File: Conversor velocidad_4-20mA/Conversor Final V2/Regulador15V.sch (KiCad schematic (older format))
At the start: 4 parts

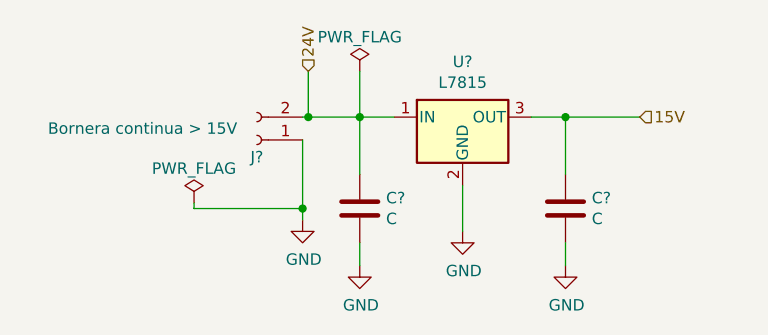
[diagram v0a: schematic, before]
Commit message: Modificacion
Modifique los esquematicos para que no de tanto error. Igualmente da error de puenteo de salidas entre las compuertas "OR" y 2 errores mas en el regulador
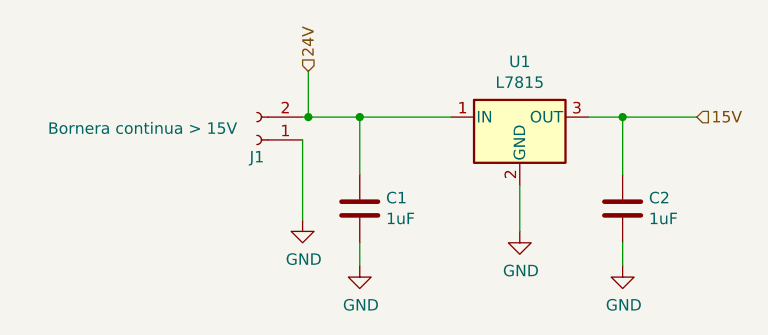
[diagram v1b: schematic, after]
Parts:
- C1, C2: renamed from C?; value C -> 1uF
- gave numbers to parts that had none: 2
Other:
- moved on the sheet: C2, U1
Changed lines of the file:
@@
 $EndDescr
 $Comp
-L Regulator_Linear:L7815 U?
+L Regulator_Linear:L7815 U1
 U 1 1 612EE8D8
-P 5625 3200
-F 0 "U?" H 5625 3442 50  0000 C CNN
-F 1 "L7815" H 5625 3351 50  0000 C CNN
-F 2 "" H 5650 3050 50  0001 L CIN
-F 3 "http://www.st.com/content/ccc/resource/technical/document/datasheet/41/4f/b3/b0/12/d4/47/88/CD00000444.pdf/files/CD00000444.pdf/jcr:content/translations/en.CD00000444.pdf" H 5625 3150 50  0001 C CNN
-	1    5625 3200
+P 5875 3200
+F 0 "U1" H 5875 3442 50  0000 C CNN
+F 1 "L7815" H 5875 3351 50  0000 C CNN
+F 2 "" H 5900 3050 50  0001 L CIN
+F 3 "http://www.st.com/content/ccc/resource/technical/document/datasheet/41/4f/b3/b0/12/d4/47/88/CD00000444.pdf/files/CD00000444.pdf/jcr:content/translations/en.CD00000444.pdf" H 5875 3150 50  0001 C CNN
+	1    5875 3200
 	1    0    0    -1
 $EndComp
 $Comp
-L power:GND #PWR?
+L power:GND #PWR0112
 U 1 1 612EE8DE
-P 5625 3700
-F 0 "#PWR?" H 5625 3450 50  0001 C CNN
-F 1 "GND" H 5630 3527 50  0000 C CNN
-F 2 "" H 5625 3700 50  0001 C CNN
-F 3 "" H 5625 3700 50  0001 C CNN
-	1    5625 3700
+P 5875 3700
+F 0 "#PWR0112" H 5875 3450 50  0001 C CNN
+F 1 "GND" H 5880 3527 50  0000 C CNN
+F 2 "" H 5875 3700 50  0001 C CNN
+F 3 "" H 5875 3700 50  0001 C CNN
+	1    5875 3700
 	1    0    0    -1
 $EndComp
 $Comp
-L Device:C C?
+L Device:C C1
 U 1 1 612EE8E4
 P 5175 3600
-F 0 "C?" H 5290 3646 50  0000 L CNN
-F 1 "C" H 5290 3555 50  0000 L CNN
+F 0 "C1" H 5290 3646 50  0000 L CNN
+F 1 "1uF" H 5290 3555 50  0000 L CNN
 F 2 "" H 5213 3450 50  0001 C CNN
 F 3 "~" H 5175 3600 50  0001 C CNN
@@
 $EndComp
 $Comp
-L Device:C C?
+L Device:C C2
 U 1 1 612EE8EA
-P 6075 3600
-F 0 "C?" H 6190 3646 50  0000 L CNN
-F 1 "C" H 6190 3555 50  0000 L CNN
-F 2 "" H 6113 3450 50  0001 C CNN
-F 3 "~" H 6075 3600 50  0001 C CNN
-	1    6075 3600
+P 6325 3600
+F 0 "C2" H 6440 3646 50  0000 L CNN
+F 1 "1uF" H 6440 3555 50  0000 L CNN
+F 2 "" H 6363 3450 50  0001 C CNN
+F 3 "~" H 6325 3600 50  0001 C CNN
+	1    6325 3600
 	1    0    0    -1
 $EndComp
 $Comp
-L Connector:Conn_01x02_Female J?
+L Connector:Conn_01x02_Female J1
 U 1 1 612EE8F0
 P 4725 3300
-F 0 "J?" H 4725 3375 50  0000 C CNN
+F 0 "J1" H 4725 3375 50  0000 C CNN
 F 1 "Bornera continua > 15V" H 5225 3250 50  0000 C CNN
 F 2 "" H 4725 3300 50  0001 C CNN
@@
 $EndComp
 Wire Wire Line
-	5325 3200 5175 3200
+	5175 3450 5175 3200
 Wire Wire Line
-	5175 3450 5175 3200
-Connection ~ 5175 3200
-Wire Wire Line
-	6075 3200 6075 3450
+	6325 3200 6325 3450
 $Comp
-L power:GND #PWR?
+L power:GND #PWR0113
 U 1 1 612EE8FB
-P 6075 3850
-F 0 "#PWR?" H 6075 3600 50  0001 C CNN
-F 1 "GND" H 6080 3677 50  0000 C CNN
-F 2 "" H 6075 3850 50  0001 C CNN
-F 3 "" H 6075 3850 50  0001 C CNN
-	1    6075 3850
+P 6325 3850
+F 0 "#PWR0113" H 6325 3600 50  0001 C CNN
+F 1 "GND" H 6330 3677 50  0000 C CNN
+F 2 "" H 6325 3850 50  0001 C CNN
+F 3 "" H 6325 3850 50  0001 C CNN
+	1    6325 3850
 	1    0    0    -1
 $EndComp
 $Comp
-L power:GND #PWR?
+L power:GND #PWR0114
 U 1 1 612EE901
 P 5175 3850
-F 0 "#PWR?" H 5175 3600 50  0001 C CNN
+F 0 "#PWR0114" H 5175 3600 50  0001 C CNN
 F 1 "GND" H 5180 3677 50  0000 C CNN
 F 2 "" H 5175 3850 50  0001 C CNN
@@
 $EndComp
 Wire Wire Line
-	5625 3500 5625 3700
+	5875 3500 5875 3700
 Wire Wire Line
-	6075 3750 6075 3850
+	6325 3750 6325 3850
 Wire Wire Line
 	5175 3750 5175 3850
 $Comp
-L power:GND #PWR?
+L power:GND #PWR0115
 U 1 1 612EE90B
 P 4925 3650
-F 0 "#PWR?" H 4925 3400 50  0001 C CNN
+F 0 "#PWR0115" H 4925 3400 50  0001 C CNN
 F 1 "GND" H 4930 3477 50  0000 C CNN
 F 2 "" H 4925 3650 50  0001 C CNN
 F 3 "" H 4925 3650 50  0001 C CNN
 	1    4925 3650
-	1    0    0    -1
-$EndComp
-$Comp
-L power:PWR_FLAG #FLG?
-U 1 1 612EE913
-P 4450 3575
-F 0 "#FLG?" H 4450 3650 50  0001 C CNN
-F 1 "PWR_FLAG" H 4450 3725 50  0000 C CNN
-F 2 "" H 4450 3575 50  0001 C CNN
-F 3 "~" H 4450 3575 50  0001 C CNN
-	1    4450 3575
-	1    0    0    -1
-$EndComp
-Wire Wire Line
-	4925 3300 4925 3600
-Wire Wire Line
-	4450 3575 4450 3600
-Wire Wire Line
-	4450 3600 4925 3600
-Connection ~ 4925 3600
-Wire Wire Line
-	4925 3600 4925 3650
-$Comp
-L power:PWR_FLAG #FLG?
-U 1 1 612EE924
-P 5175 3000
-F 0 "#FLG?" H 5175 3075 50  0001 C CNN
-F 1 "PWR_FLAG" H 5175 3150 50  0000 C CNN
-F 2 "" H 5175 3000 50  0001 C CNN
-F 3 "~" H 5175 3000 50  0001 C CNN
-	1    5175 3000
 	1    0    0    -1
 $EndComp
@@
 Wire Wire Line
 	4950 3200 5175 3200
-Wire Wire Line
-	5175 3000 5175 3200
-Text HLabel 6400 3200 2    50   Input ~ 0
+Text HLabel 6650 3200 2    50   Input ~ 0
 15V
 Wire Wire Line
-	5925 3200 6075 3200
-Connection ~ 6075 3200
+	6175 3200 6325 3200
+Connection ~ 6325 3200
 Wire Wire Line
-	6075 3200 6400 3200
+	6325 3200 6650 3200
 Text HLabel 4950 3000 1    50   Input ~ 0
 24V
 Wire Wire Line
 	4950 3000 4950 3200
+Wire Wire Line
+	4925 3300 4925 3650
+Wire Wire Line
+	5175 3200 5575 3200
+Connection ~ 5175 3200
 $EndSCHEMATC

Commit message: Agregue footprints
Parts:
- C1, C2: footprint (none) -> Capacitor_SMD:C_0603_1608Metric_Pad1.08x0.95mm_HandSolder
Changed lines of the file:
@@
 F 0 "C1" H 5290 3646 50  0000 L CNN
 F 1 "1uF" H 5290 3555 50  0000 L CNN
-F 2 "" H 5213 3450 50  0001 C CNN
+F 2 "Capacitor_SMD:C_0603_1608Metric_Pad1.08x0.95mm_HandSolder" H 5213 3450 50  0001 C CNN
 F 3 "~" H 5175 3600 50  0001 C CNN
 	1    5175 3600
@@
 F 0 "C2" H 6440 3646 50  0000 L CNN
 F 1 "1uF" H 6440 3555 50  0000 L CNN
-F 2 "" H 6363 3450 50  0001 C CNN
+F 2 "Capacitor_SMD:C_0603_1608Metric_Pad1.08x0.95mm_HandSolder" H 6363 3450 50  0001 C CNN
 F 3 "~" H 6325 3600 50  0001 C CNN
 	1    6325 3600

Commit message: Actualizacion Esquematico en bloques
Agregue un par de footprints y acomodé el relé en el bloque correspondiente. Hay que consultar sobre los footprint del 4040 y 4070
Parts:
- U1: footprint (none) -> Package_TO_SOT_SMD:TO-263-3_TabPin2
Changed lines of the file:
@@
 F 0 "U1" H 5875 3442 50  0000 C CNN
 F 1 "L7815" H 5875 3351 50  0000 C CNN
-F 2 "" H 5900 3050 50  0001 L CIN
-F 3 "http://www.st.com/content/ccc/resource/technical/document/datasheet/41/4f/b3/b0/12/d4/47/88/CD00000444.pdf/files/CD00000444.pdf/jcr:content/translations/en.CD00000444.pdf" H 5875 3150 50  0001 C CNN
+F 2 "Package_TO_SOT_SMD:TO-263-3_TabPin2" H 5900 3050 50  0001 L CIN
+F 3 "https://www.digikey.com/es/products/detail/stmicroelectronics/L7815ACD2T-TR/1663423" H 5875 3150 50  0001 C CNN
 	1    5875 3200
 	1    0    0    -1
